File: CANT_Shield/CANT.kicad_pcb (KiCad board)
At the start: 2 copper layers, 55.9 x 36.8 mm, 12 parts, among them CN7 CN7, CN8 CN8, J1 Screw_Terminal_01x02, U1 SN65HVD232

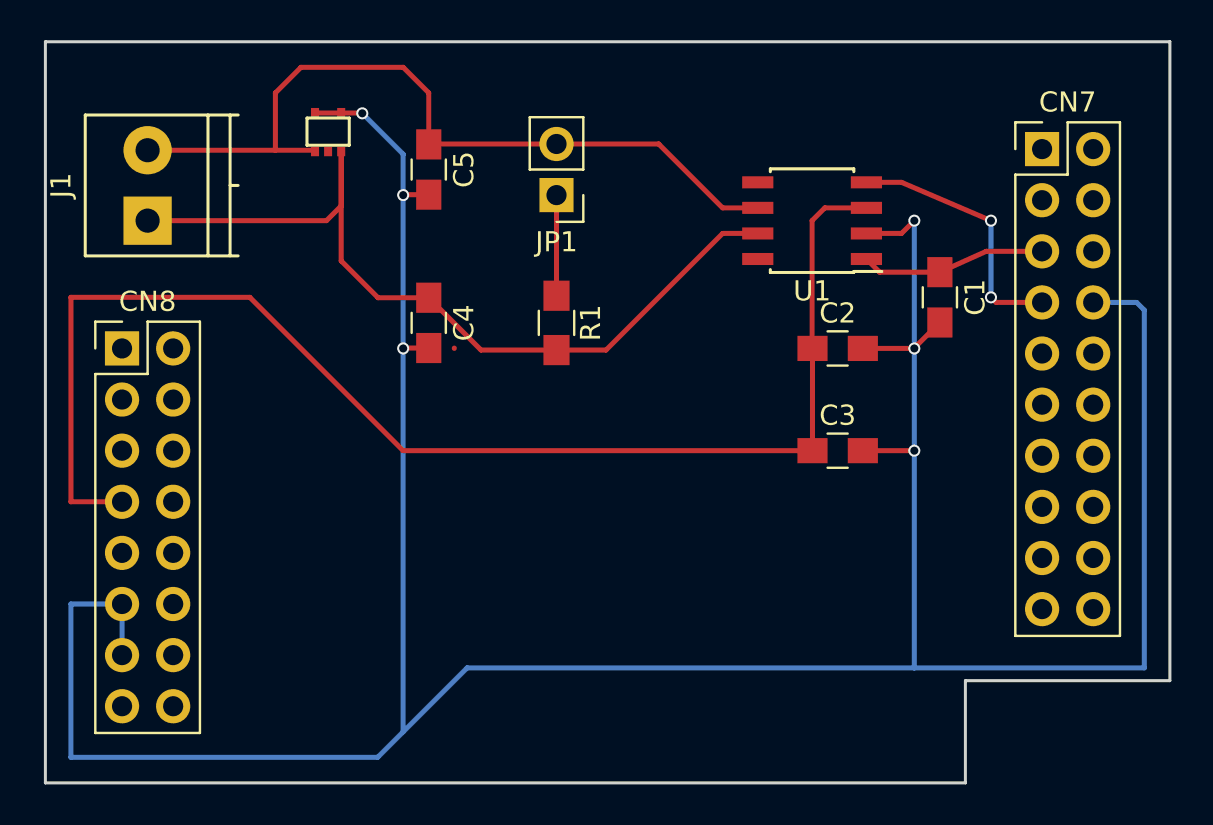
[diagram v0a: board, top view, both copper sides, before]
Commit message: Version 0.1 of shield, with analog switch
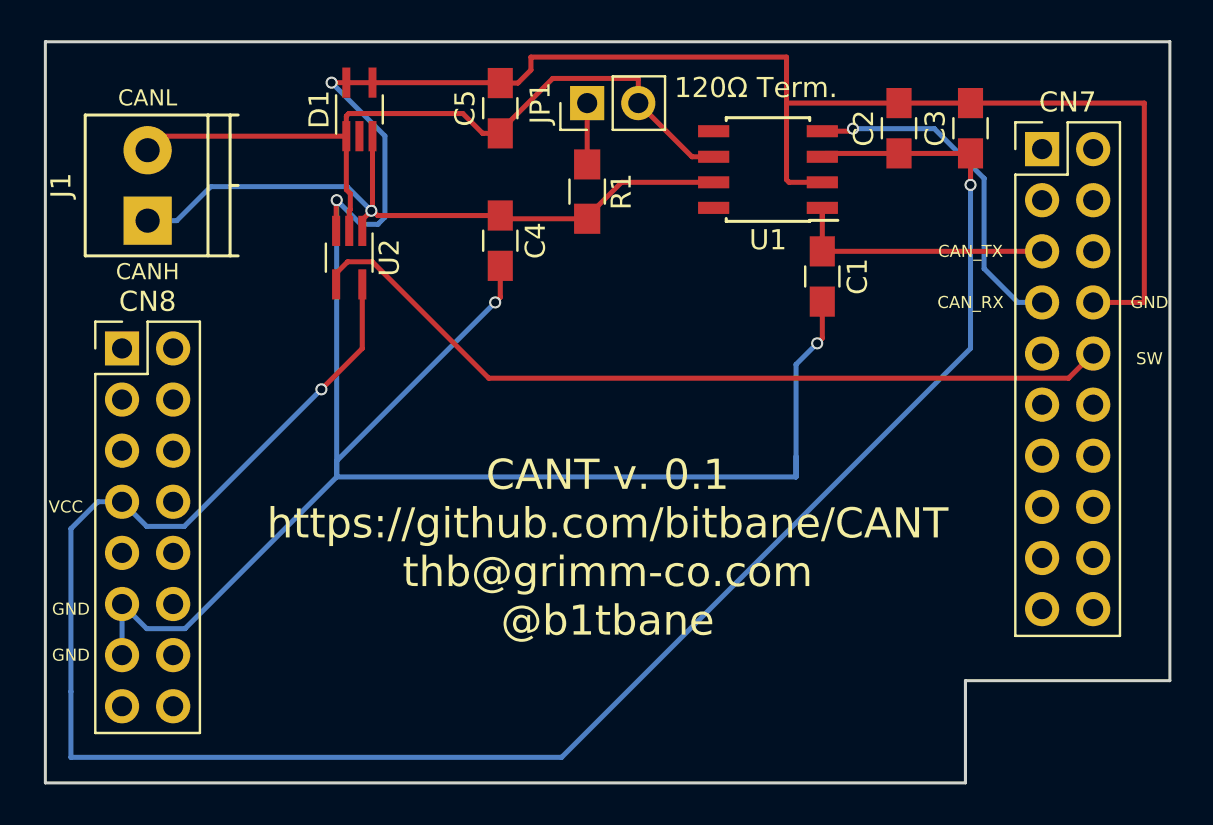
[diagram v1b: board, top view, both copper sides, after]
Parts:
- added G***: LOGO, SP1002_02:LOGO, F.Cu at (0.00, 0.00)
- added G*** (x5): LOGO, LOGO, F.Cu at (0.00, 0.00)
- added G***: LOGO, SP1002_02:LOGO, B.Cu at (146.3, 134.4)
- added U2: 74LVC1G66, TO_SOT_Packages_SMD:SOT-353_SC-70-5_Handsoldering, F.Cu at (135.7, 122.5)
- D1: footprint SP1002_02:SP1002-02 -> TO_SOT_Packages_SMD:SOT-353_SC-70-5_Handsoldering
- moved C3 17.3 mm to (166.6, 116.1), turned to 90 degrees
- moved C2 11.4 mm to (163.1, 116.1), turned to 90 degrees
- moved R1 6.70 mm to (147.6, 119.2)
- moved C1 5.93 mm to (159.3, 123.4)
- moved C4 5.42 mm to (143.3, 121.6)
- moved JP1 4.82 mm to (147.6, 114.8), turned to 90 degrees
- moved C5 4.68 mm to (143.3, 115.1), turned to 90 degrees
- moved U1 3.36 mm to (156.6, 118.1)
- moved D1 2.60 mm to (136.3, 115.1), turned to 90 degrees
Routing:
- net Net-(CN7-Pad10): track 0.00 -> 41.3 mm
- net VCC: track 67.1 -> 104.0 mm, vias 0 -> 2
- net Net-(C4-Pad1): track 43.0 -> 35.2 mm, vias 0 -> 1
- net GND: track 156.7 -> 151.6 mm, vias 6 -> 4
- net CAN_TX: track 9.22 -> 13.6 mm
- net CAN_RX: track 13.0 -> 17.2 mm, vias 2 -> 1
- net Net-(C5-Pad1): track 40.7 -> 38.2 mm
- net Net-(JP1-Pad1): track 5.00 -> 3.05 mm
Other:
- board text added: "120Ω Term."
- board text added: "CANH"
- board text added: "CANL"
- board text added: "CANT v. 0.1 https://github.com/bitbane/CANT thb@grimm-co.com @b1tbane"
- board text added: "CAN_RX"
- board text added: "CAN_TX"
- board text added: "GND"
- board text added: "SW"
- board text added: "VCC"
- board text added: "https://www.grimm-co.com @grimmcyber"

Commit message: Added board name to silkscreen
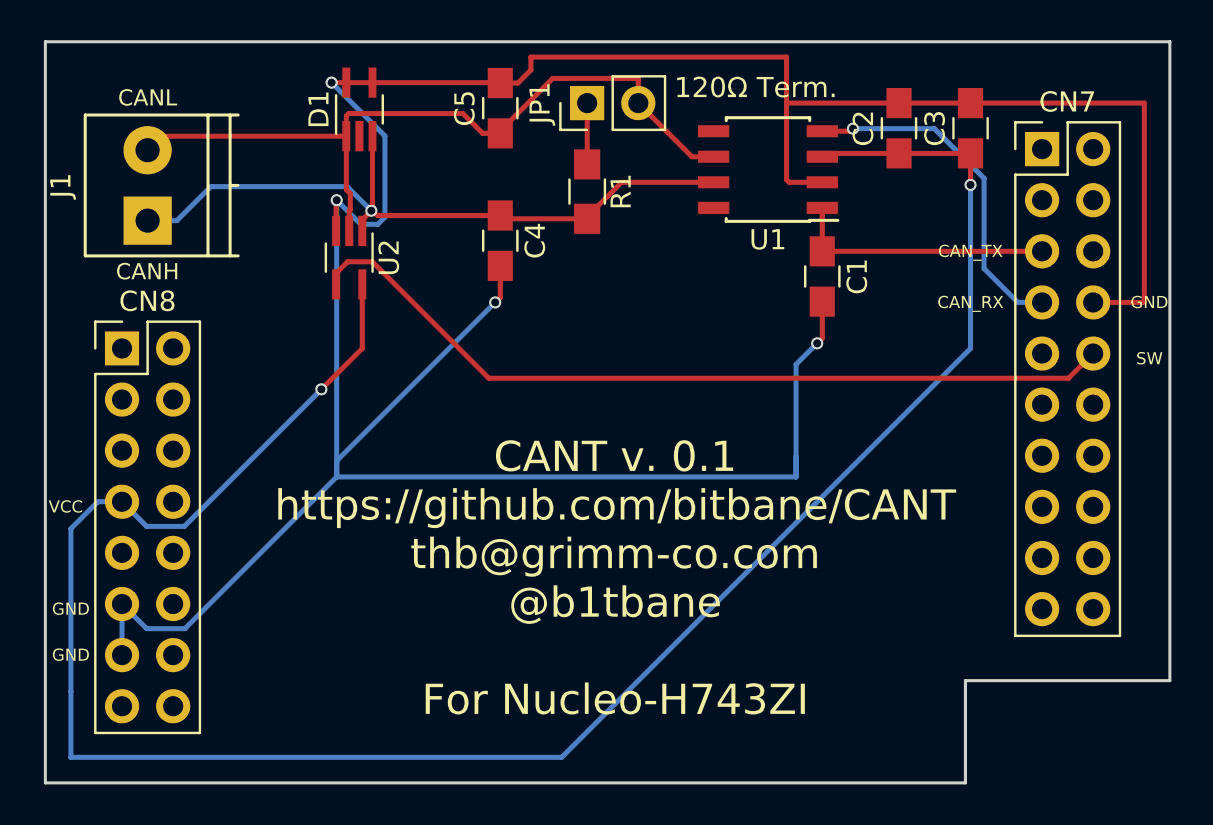
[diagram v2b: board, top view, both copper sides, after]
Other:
- board text added: "CANT v. 0.1 https://github.com/bitbane/CANT thb@grimm-co.com @b1tbane For Nucleo-H743ZI"
- board text removed: "CANT v. 0.1 https://github.com/bitbane/CANT thb@grimm-co.com @b1tbane"
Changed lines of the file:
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@@
     (effects (font (size 1 1) (thickness 0.2)))
   )
-  (gr_text "CANT v. 0.1\nhttps://github.com/bitbane/CANT\nthb@grimm-co.com\n@b1tbane\n" (at 148.59 136.906) (layer F.SilkS)
+  (gr_text "CANT v. 0.1\nhttps://github.com/bitbane/CANT\nthb@grimm-co.com\n@b1tbane\n\nFor Nucleo-H743ZI" (at 148.971 138.43) (layer F.SilkS)
     (effects (font (size 1.5 1.5) (thickness 0.3)))
   )

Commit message: Changed to rev 0.2, switched to using TJA1051 CAN transceiver
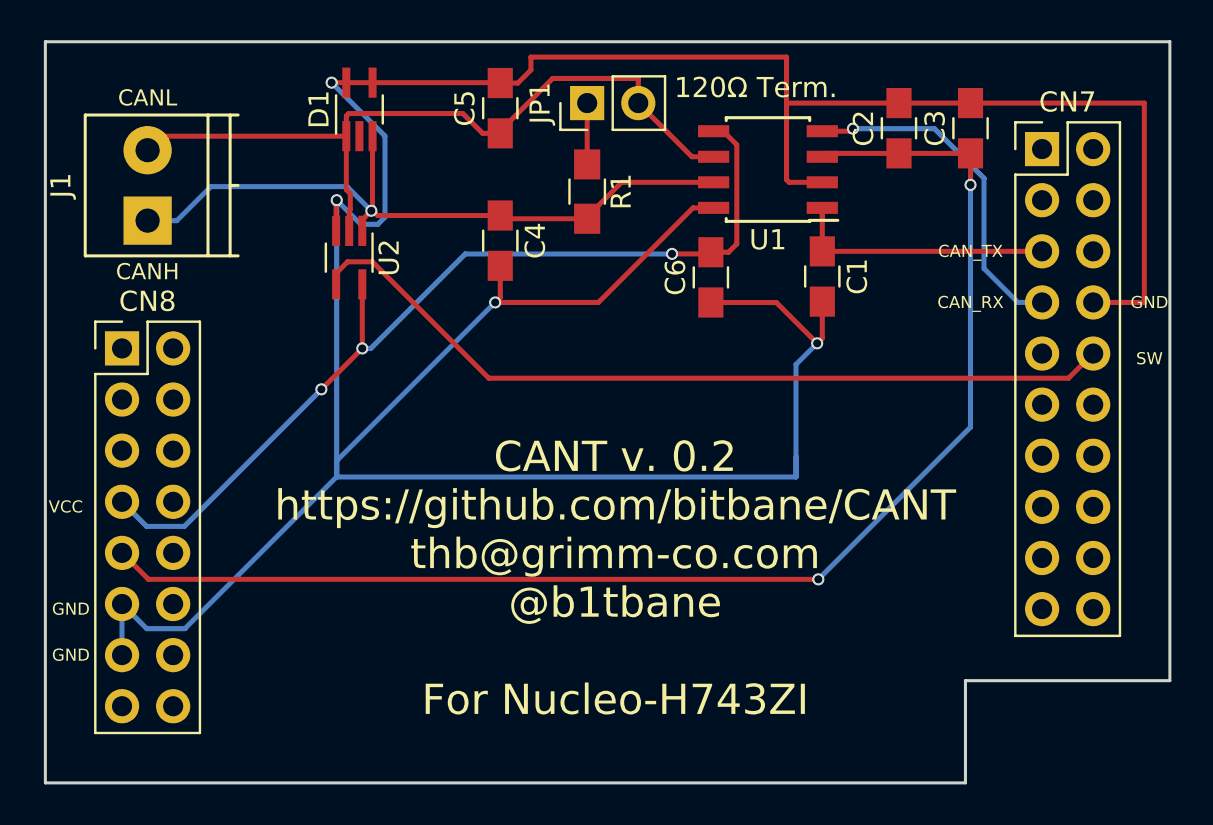
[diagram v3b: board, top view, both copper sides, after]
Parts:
- removed the G*** at (0.00, 0.00) (x6)
- removed the G*** at (146.3, 134.4)
- added C6: 0.1uF, Capacitors_SMD:C_0805_HandSoldering, F.Cu at (153.7, 123.5)
- added G***: LOGO, SP1002_02:LOGO, B.Cu at (147.3, 134.3)
- U1: value SN65HVD232 -> TJA1051T_3
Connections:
- C2 pad 1: VCC -> 5V
- C3 pad 1: VCC -> 5V
- CN8 pad 9: Net-(CN8-Pad9) -> 5V
- U1 pad 3: VCC -> 5V
- U1 pad 5: Net-(U1-Pad5) -> VCC
- U1 pad 8: Net-(U1-Pad8) -> GND
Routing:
- net 5V: track 0.00 -> 66.9 mm, vias 0 -> 2
- net VCC: track 104.0 -> 46.4 mm, vias 2 -> 3
- net GND: track 151.6 -> 170.5 mm
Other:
- board text added: "CANT v. 0.2 https://github.com/bitbane/CANT thb@grimm-co.com @b1tbane For Nucleo-H743ZI"
- board text removed: "CANT v. 0.1 https://github.com/bitbane/CANT thb@grimm-co.com @b1tbane For Nucleo-H743ZI"

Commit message: Finished with rev 0.2 of the CANT shield, mostly a redesign for the much cheaper TJA1051T/3
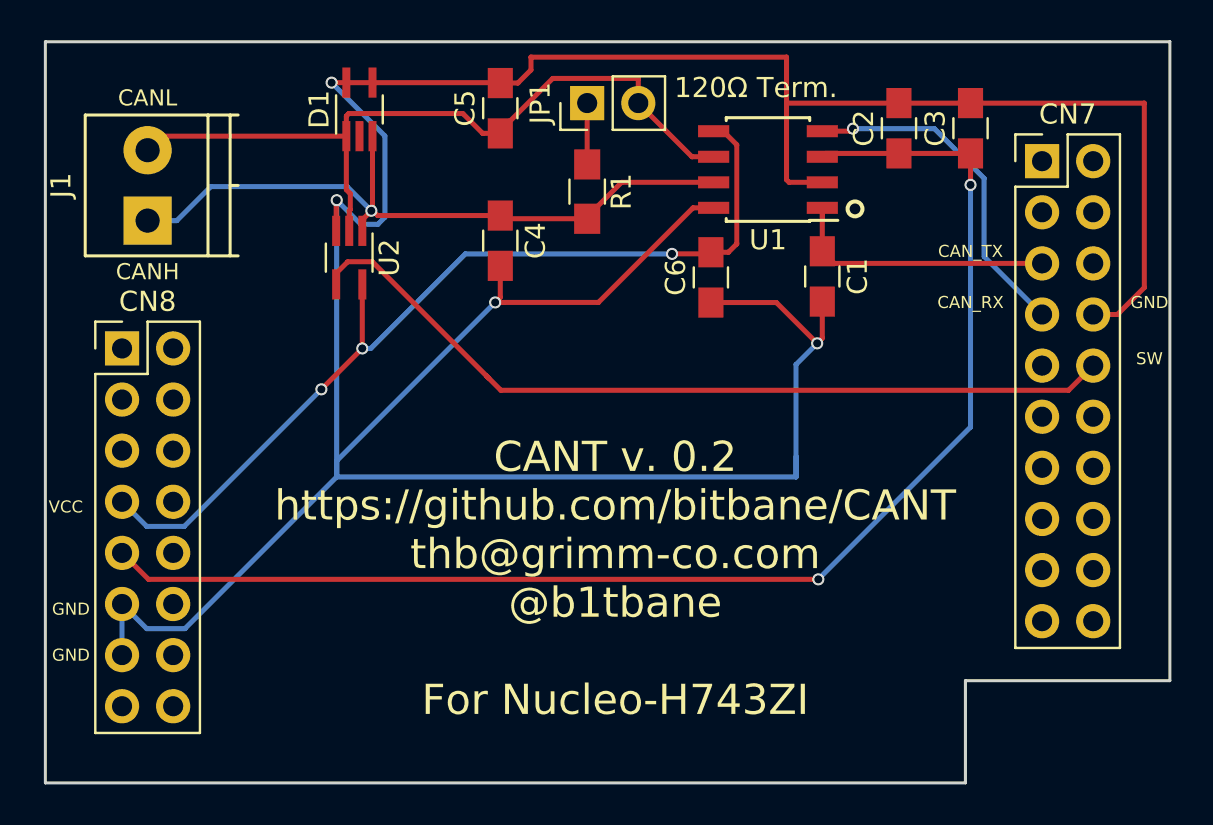
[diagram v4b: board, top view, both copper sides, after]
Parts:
- moved CN7 0.60 mm to (170.2, 117.7)
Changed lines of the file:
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@@
   (general
     (thickness 1.6)
-    (drawings 18)
-    (tracks 142)
+    (drawings 19)
+    (tracks 145)
     (zones 0)
     (modules 15)
@@
     (0 F.Cu signal)
     (31 B.Cu signal)
-    (32 B.Adhes user)
-    (33 F.Adhes user)
-    (34 B.Paste user)
-    (35 F.Paste user)
-    (36 B.SilkS user)
+    (32 B.Adhes user hide)
+    (33 F.Adhes user hide)
+    (34 B.Paste user hide)
+    (35 F.Paste user hide)
+    (36 B.SilkS user hide)
     (37 F.SilkS user)
-    (38 B.Mask user)
-    (39 F.Mask user)
-    (40 Dwgs.User user)
-    (41 Cmts.User user)
-    (42 Eco1.User user)
-    (43 Eco2.User user)
+    (38 B.Mask user hide)
+    (39 F.Mask user hide)
+    (40 Dwgs.User user hide)
+    (41 Cmts.User user hide)
+    (42 Eco1.User user hide)
+    (43 Eco2.User user hide)
     (44 Edge.Cuts user)
     (45 Margin user)
-    (46 B.CrtYd user)
+    (46 B.CrtYd user hide)
     (47 F.CrtYd user)
-    (48 B.Fab user)
-    (49 F.Fab user)
+    (48 B.Fab user hide)
+    (49 F.Fab user hide)
   )
   (setup
@@
   )
   (module Pin_Headers:Pin_Header_Straight_2x10_Pitch2.54mm (layer F.Cu)
-    (at 170.18 117.094)
+    (at 170.18 117.694)
     (descr "Through hole straight pin header, 2x10, 2.54mm pitch, double rows")
     (tags "Through hole pin header THT 2x10 2.54mm double row")
@@
       (xy -3.762783 -0.746721)) (layer B.SilkS) (width 0.01))
   )
+  (gr_circle (center 160.8836 120.0658) (end 161.2392 120.1674) (layer F.SilkS) (width 0.2))
   (gr_text "CANT v. 0.2\nhttps://github.com/bitbane/CANT\nthb@grimm-co.com\n@b1tbane\n\nFor Nucleo-H743ZI" (at 148.971 138.43) (layer F.SilkS)
     (effects (font (size 1.5 1.5) (thickness 0.3)))
@@
   (gr_line (start 120.65 111.76) (end 176.53 111.76) (angle 90) (layer Edge.Cuts) (width 0.15))
   (segment (start 159.258 120.565) (end 159.258 120.015) (width 0.25) (layer F.Cu) (net 1))
-  (segment (start 170.18 122.174) (end 159.258 122.174) (width 0.25) (layer F.Cu) (net 1))
   (segment (start 159.258 122.174) (end 159.258 120.015) (width 0.25) (layer F.Cu) (net 1))
+  (segment (start 159.858 122.774) (end 159.258 122.174) (width 0.25) (layer F.Cu) (net 1))
+  (segment (start 170.18 122.774) (end 159.858 122.774) (width 0.25) (layer F.Cu) (net 1))
   (segment (start 124.46 142.24) (end 124.46 139.7) (width 0.25) (layer B.Cu) (net 2))
-  (segment (start 175.26 124.714) (end 172.72 124.714) (width 0.25) (layer F.Cu) (net 2))
   (segment (start 166.624 114.808) (end 175.26 114.808) (width 0.25) (layer F.Cu) (net 2))
-  (segment (start 175.26 114.808) (end 175.26 124.714) (width 0.25) (layer F.Cu) (net 2))
   (segment (start 166.624 114.808) (end 163.068 114.808) (width 0.25) (layer F.Cu) (net 2))
   (segment (start 157.48 118.618) (end 157.48 114.808) (width 0.25) (layer F.Cu) (net 2))
@@
   (segment (start 148.134 124.714) (end 143.426264 124.714) (width 0.25) (layer F.Cu) (net 2))
   (segment (start 153.858 120.015) (end 152.833 120.015) (width 0.25) (layer F.Cu) (net 2))
+  (segment (start 175.26 123.976081) (end 175.26 114.808) (width 0.25) (layer F.Cu) (net 2))
+  (segment (start 173.922081 125.314) (end 175.26 123.976081) (width 0.25) (layer F.Cu) (net 2))
+  (segment (start 172.72 125.314) (end 173.922081 125.314) (width 0.25) (layer F.Cu) (net 2))
   (segment (start 125.685001 135.845001) (end 127.552999 135.845001) (width 0.25) (layer B.Cu) (net 3))
   (segment (start 124.46 134.62) (end 125.685001 135.845001) (width 0.25) (layer B.Cu) (net 3))
@@
   (segment (start 136.398 127) (end 136.398 127) (width 0.25) (layer F.Cu) (net 3))
   (segment (start 136.398 123.818) (end 136.398 127) (width 0.25) (layer F.Cu) (net 3))
-  (segment (start 166.624 118.872) (end 166.624 118.872) (width 0.25) (layer B.Cu) (net 38))
-  (via (at 166.624 118.872) (size 0.6) (drill 0.4) (layers F.Cu B.Cu) (net 38))
-  (segment (start 166.624 117.308) (end 166.624 118.872) (width 0.25) (layer F.Cu) (net 38))
-  (segment (start 166.624 117.308) (end 163.068 117.308) (width 0.25) (layer F.Cu) (net 38))
-  (segment (start 159.425 117.308) (end 159.258 117.475) (width 0.25) (layer F.Cu) (net 38))
-  (segment (start 163.068 117.308) (end 159.425 117.308) (width 0.25) (layer F.Cu) (net 38))
   (segment (start 154.333 116.205) (end 153.858 116.205) (width 0.25) (layer F.Cu) (net 3))
   (segment (start 155.008001 116.880001) (end 154.333 116.205) (width 0.25) (layer F.Cu) (net 3))
@@
   (segment (start 135.606 116.452) (end 126.428 116.452) (width 0.25) (layer F.Cu) (net 5))
   (segment (start 167.299001 118.547999) (end 164.829002 116.078) (width 0.25) (layer B.Cu) (net 11))
-  (segment (start 167.299001 123.035082) (end 167.299001 118.547999) (width 0.25) (layer B.Cu) (net 11))
-  (segment (start 170.18 124.714) (end 168.977919 124.714) (width 0.25) (layer B.Cu) (net 11))
-  (segment (start 168.977919 124.714) (end 167.299001 123.035082) (width 0.25) (layer B.Cu) (net 11))
   (segment (start 164.829002 116.078) (end 160.782 116.078) (width 0.25) (layer B.Cu) (net 11))
   (segment (start 160.782 116.078) (end 160.782 116.078) (width 0.25) (layer B.Cu) (net 11))
@@
   (segment (start 160.655 116.205) (end 160.782 116.078) (width 0.25) (layer F.Cu) (net 11))
   (segment (start 159.258 116.205) (end 160.655 116.205) (width 0.25) (layer F.Cu) (net 11))
+  (segment (start 167.299001 122.433001) (end 170.18 125.314) (width 0.25) (layer B.Cu) (net 11))
+  (segment (start 167.299001 118.547999) (end 167.299001 122.433001) (width 0.25) (layer B.Cu) (net 11))
   (segment (start 135.098 123.268) (end 135.098 123.818) (width 0.25) (layer F.Cu) (net 13))
   (segment (start 135.673001 122.692999) (end 135.098 123.268) (width 0.25) (layer F.Cu) (net 13))
   (segment (start 136.898001 122.692999) (end 135.673001 122.692999) (width 0.25) (layer F.Cu) (net 13))
-  (segment (start 142.684003 128.479001) (end 136.898001 122.692999) (width 0.25) (layer F.Cu) (net 13))
-  (segment (start 171.494999 128.479001) (end 142.684003 128.479001) (width 0.25) (layer F.Cu) (net 13))
-  (segment (start 172.72 127.254) (end 171.494999 128.479001) (width 0.25) (layer F.Cu) (net 13))
+  (segment (start 143.284003 129.079001) (end 142.5702 128.365198) (width 0.25) (layer F.Cu) (net 13))
+  (segment (start 171.494999 129.079001) (end 143.284003 129.079001) (width 0.25) (layer F.Cu) (net 13))
+  (segment (start 172.72 127.854) (end 171.494999 129.079001) (width 0.25) (layer F.Cu) (net 13))
+  (segment (start 142.684003 128.479001) (end 142.5702 128.365198) (width 0.25) (layer F.Cu) (net 13))
+  (segment (start 142.5702 128.365198) (end 136.898001 122.692999) (width 0.25) (layer F.Cu) (net 13))
   (segment (start 147.574 114.808) (end 147.574 117.856) (width 0.25) (layer F.Cu) (net 37))
+  (segment (start 166.624 118.872) (end 166.624 118.872) (width 0.25) (layer B.Cu) (net 38))
+  (via (at 166.624 118.872) (size 0.6) (drill 0.4) (layers F.Cu B.Cu) (net 38))
+  (segment (start 166.624 117.308) (end 166.624 118.872) (width 0.25) (layer F.Cu) (net 38))
+  (segment (start 166.624 117.308) (end 163.068 117.308) (width 0.25) (layer F.Cu) (net 38))
+  (segment (start 159.425 117.308) (end 159.258 117.475) (width 0.25) (layer F.Cu) (net 38))
+  (segment (start 163.068 117.308) (end 159.425 117.308) (width 0.25) (layer F.Cu) (net 38))
   (segment (start 125.774999 138.474999) (end 159.060601 138.474999) (width 0.25) (layer F.Cu) (net 38))
   (segment (start 124.46 137.16) (end 125.774999 138.474999) (width 0.25) (layer F.Cu) (net 38))
